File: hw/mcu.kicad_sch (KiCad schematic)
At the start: 3 parts, among them U3 STM32G431C6Tx, U4 STM32G441RBTx, U6 RP2040

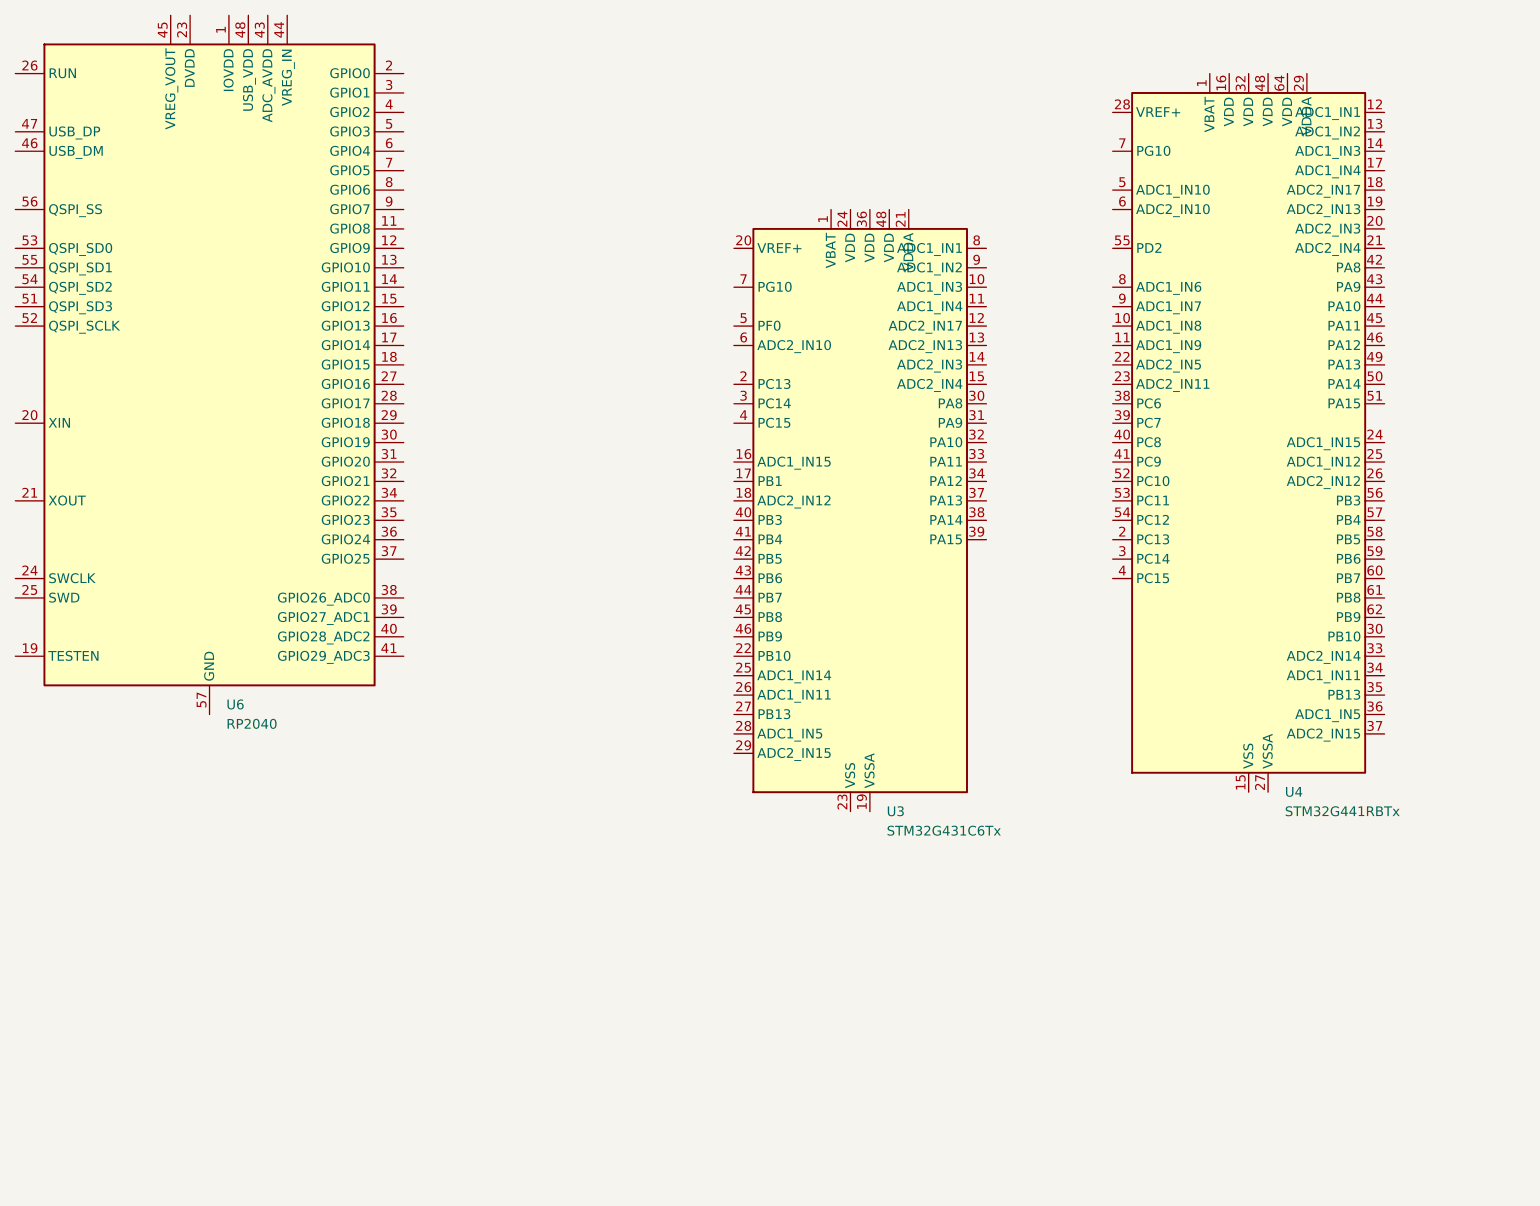
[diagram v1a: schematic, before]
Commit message: Update encoder circuit
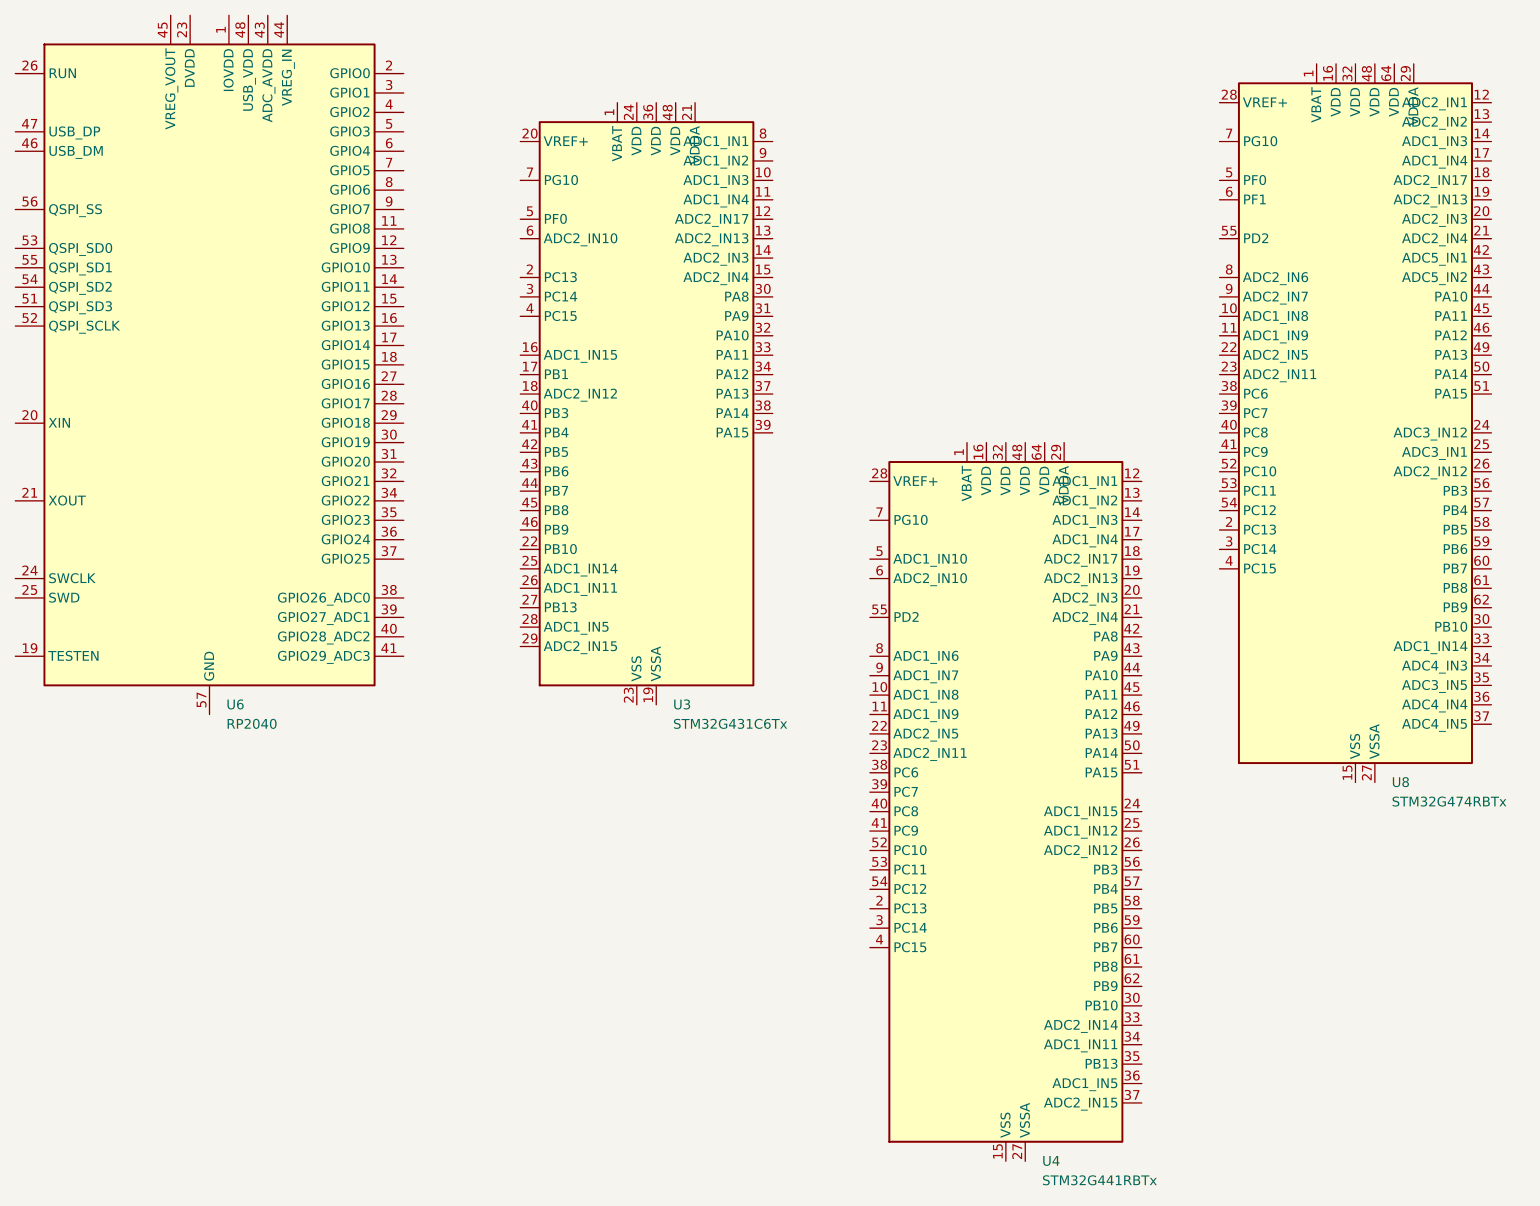
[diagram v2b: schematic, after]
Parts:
- added U8: STM32G474RBTx, Package_QFP:LQFP-64_10x10mm_P0.5mm, symbol MCU_ST_STM32G4:STM32G474RBTx
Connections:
- new net: U8.15 (VSS), U8.31 (VSS), U8.47 (VSS), U8.63 (VSS)
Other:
- moved on the sheet: U3, U4
